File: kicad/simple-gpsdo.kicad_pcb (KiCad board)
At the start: 2 copper layers, 119.5 x 74.5 mm, 93 parts, among them J2 PWR, J3 ISP, J4 GPS_NEO, J5 GPS_IN, J6 10MHz_OUT, J7 NEO-6M, J8 10MHz_OUT, J9 USB_C_Receptacle_USB2.0, SW1 RST, U1 BD50FC0FP-E2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

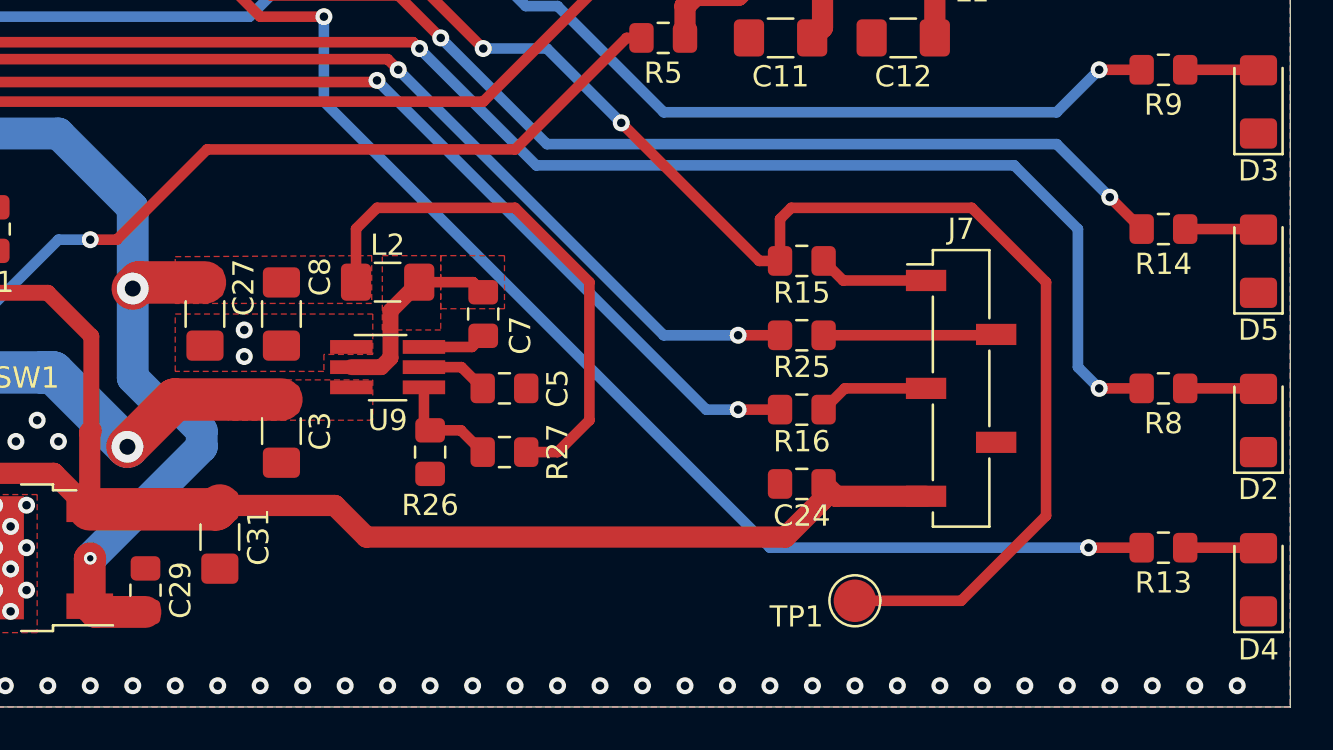
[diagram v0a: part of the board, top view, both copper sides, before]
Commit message: finalizing PCB, added 3D models
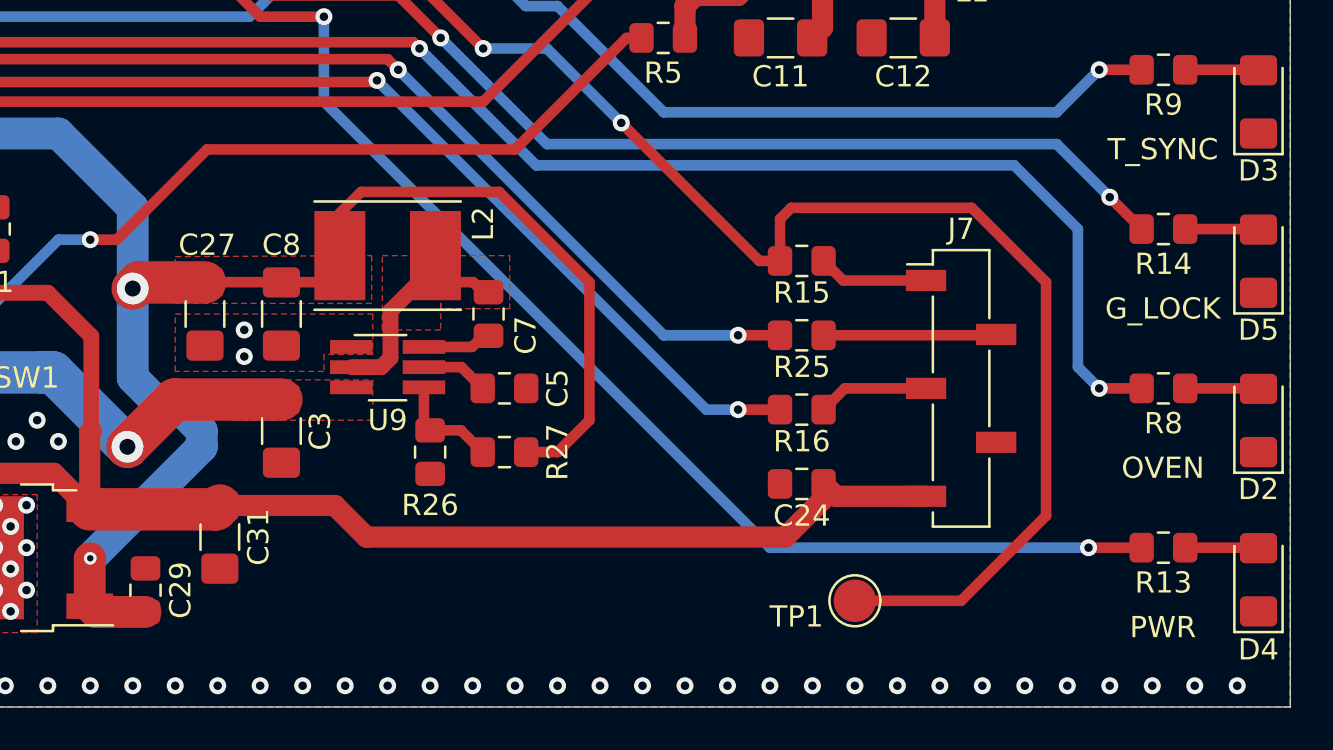
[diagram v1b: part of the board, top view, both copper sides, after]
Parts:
- L2: footprint Inductor_SMD:L_1206_3216Metric_Pad1.42x1.75mm_HandSolder -> Inductor_SMD:L_Taiyo-Yuden_NR-50xx_HandSoldering
- moved L2 1.25 mm to (152.0, 128.2)
- moved C7 0.25 mm to (156.8, 131.0)
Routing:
- net Net-(C27-Pad1): track 213.0 -> 224.2 mm
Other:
- board text added: "G_LOCK"
- board text added: "OVEN"
- board text added: "PWR"
- board text added: "T_SYNC"

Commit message: finalizing rev C PCB
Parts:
- moved J9 10.3 mm to (79.0, 122.8)
- moved R1 10.3 mm to (90.0, 121.2)
- moved R2 10.3 mm to (90.0, 124.2)
- moved J2 7.00 mm to (85.2, 130.5)
- moved F1 6.75 mm to (89.2, 130.3)
- moved FB1 6.75 mm to (93.2, 130.3)
- moved J6 2.25 mm to (91.5, 109.2)
- moved J8 2.25 mm to (91.5, 89.8)
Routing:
- net Net-(C3-Pad1): track 66.3 -> 59.9 mm
- net Net-(J9-PadA4): track 67.2 -> 61.1 mm
- net Net-(R2-Pad2): track 28.3 -> 22.6 mm
- net Net-(C27-Pad1): track 224.2 -> 229.0 mm
- net Net-(R1-Pad1): track 25.4 -> 22.7 mm
- net Net-(J8-Pad2): track 7.01 -> 9.26 mm, vias 0 -> 1
- net Net-(J6-Pad2): track 7.28 -> 9.53 mm, vias 0 -> 1
- net Net-(J8-Pad1): track 4.77 -> 2.63 mm
- net Net-(J6-Pad1): track 4.78 -> 2.66 mm
- net GND: vias 671 -> 676

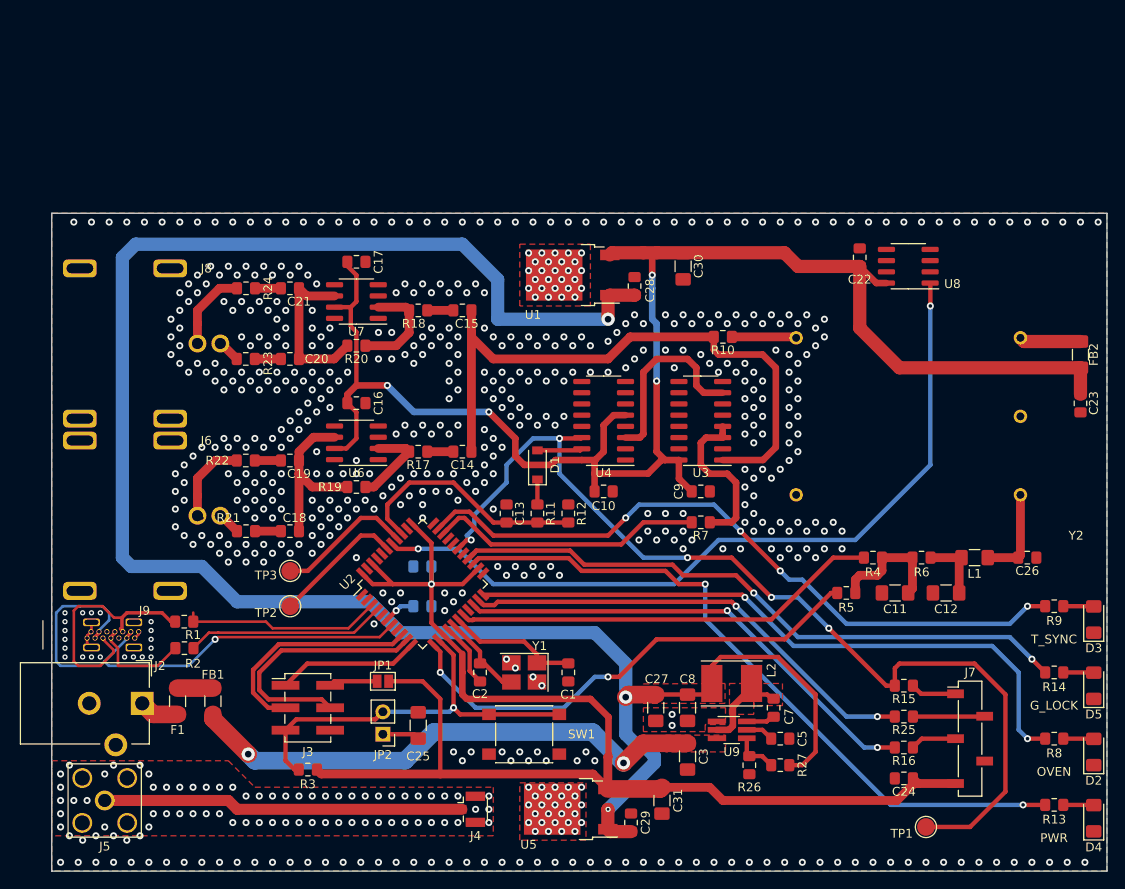
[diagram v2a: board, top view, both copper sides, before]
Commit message: added extra buck filtering
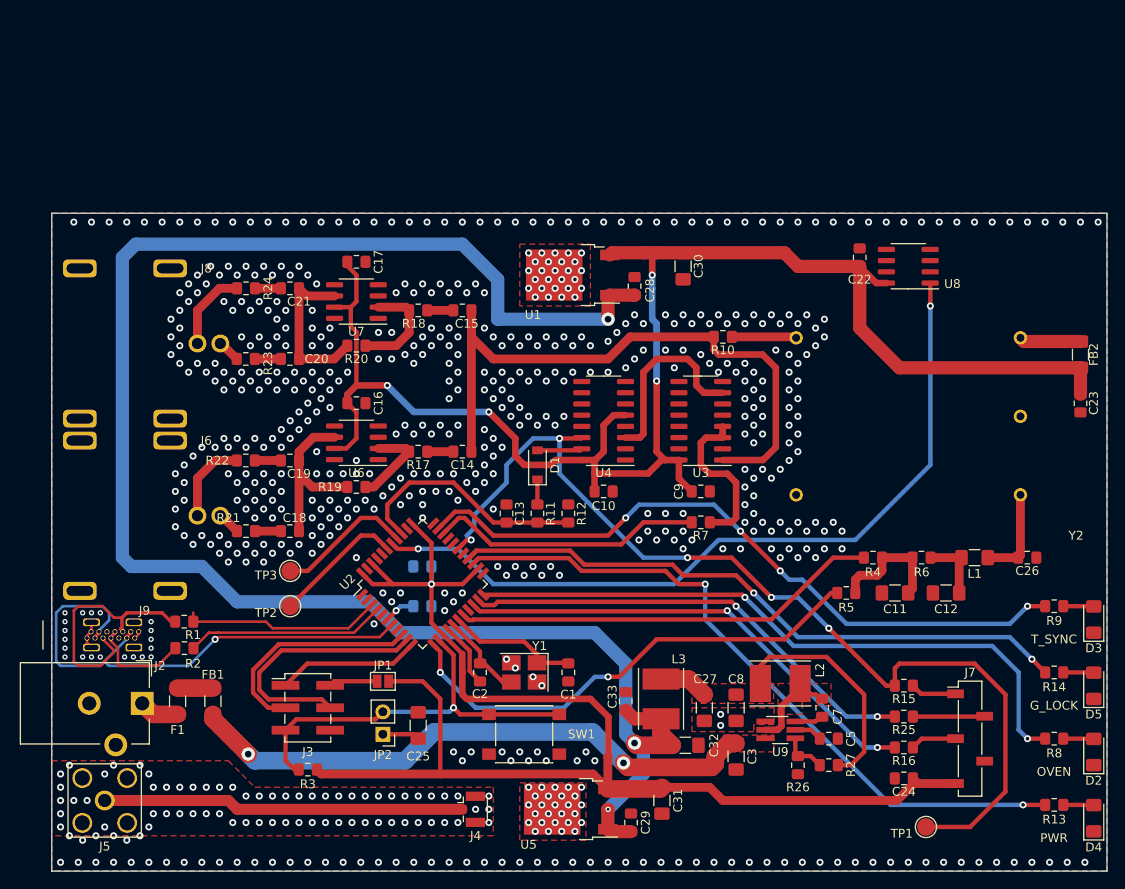
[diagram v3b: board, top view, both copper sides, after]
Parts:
- added C32: 10uF, Capacitor_SMD:C_1206_3216Metric_Pad1.42x1.75mm_HandSolder, F.Cu at (146.8, 135.2)
- added C33: 0.1uF, Capacitor_SMD:C_0805_2012Metric_Pad1.15x1.40mm_HandSolder, F.Cu at (140.0, 130.2)
- added L3: 3.3uH, Inductor_SMD:L_Taiyo-Yuden_NR-50xx_HandSoldering, F.Cu at (144.0, 130.0)
- J9: value USB_C_Receptacle_USB2.0 -> USB_C
- L1: value 33uH -> 3.3uH
- moved C27 5.50 mm to (148.9, 131.0)
- moved C3 5.50 mm to (152.5, 136.5)
- moved C5 5.50 mm to (163.0, 134.5)
- moved C7 5.50 mm to (162.2, 131.0)
- moved C8 5.50 mm to (152.5, 131.0)
- moved L2 5.50 mm to (157.5, 128.2)
- moved R26 5.50 mm to (159.5, 137.5)
- moved R27 5.50 mm to (163.0, 137.5)
- moved U9 5.50 mm to (157.5, 133.5)
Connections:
- C28 pad 2: Net-(C27-Pad1) -> +6V
- C29 pad 2: Net-(C27-Pad1) -> +6V
- U1 pad 1: Net-(C27-Pad1) -> +6V
- U5 pad 1: Net-(C27-Pad1) -> +6V
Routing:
- net +6V: track 0.00 -> 199.6 mm, vias 0 -> 3
- net Net-(C27-Pad1): track 229.0 -> 33.2 mm, vias 3 -> 0
- net Net-(C3-Pad1): track 59.9 -> 66.3 mm
- net Net-(J8-Pad2): vias 1 -> 0
- net Net-(J6-Pad2): vias 1 -> 0

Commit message: finalizing revC schematic and board
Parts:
- added J1: PPS_OUT, Connector_PinHeader_2.54mm:PinHeader_2x01_P2.54mm_Vertical, F.Cu at (95.8, 129.0)
- added Q1: DMP3099L, Package_TO_SOT_SMD:SOT-23_Handsoldering, F.Cu at (92.0, 136.5)
- moved FB1 1.00 mm to (92.2, 130.3)
- moved F1 0.25 mm to (89.0, 130.3)
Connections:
- FB1 pad 2: Net-(C3-Pad1) -> Net-(FB1-Pad2)
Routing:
- net GPS_PPS: track 112.0 -> 214.2 mm, vias 5 -> 6
- net Net-(FB1-Pad2): track 0.00 -> 5.47 mm
- net Net-(C3-Pad1): track 66.3 -> 64.2 mm
- net Net-(F1-Pad1): track 4.00 -> 3.25 mm
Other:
- board text added: "PPS"

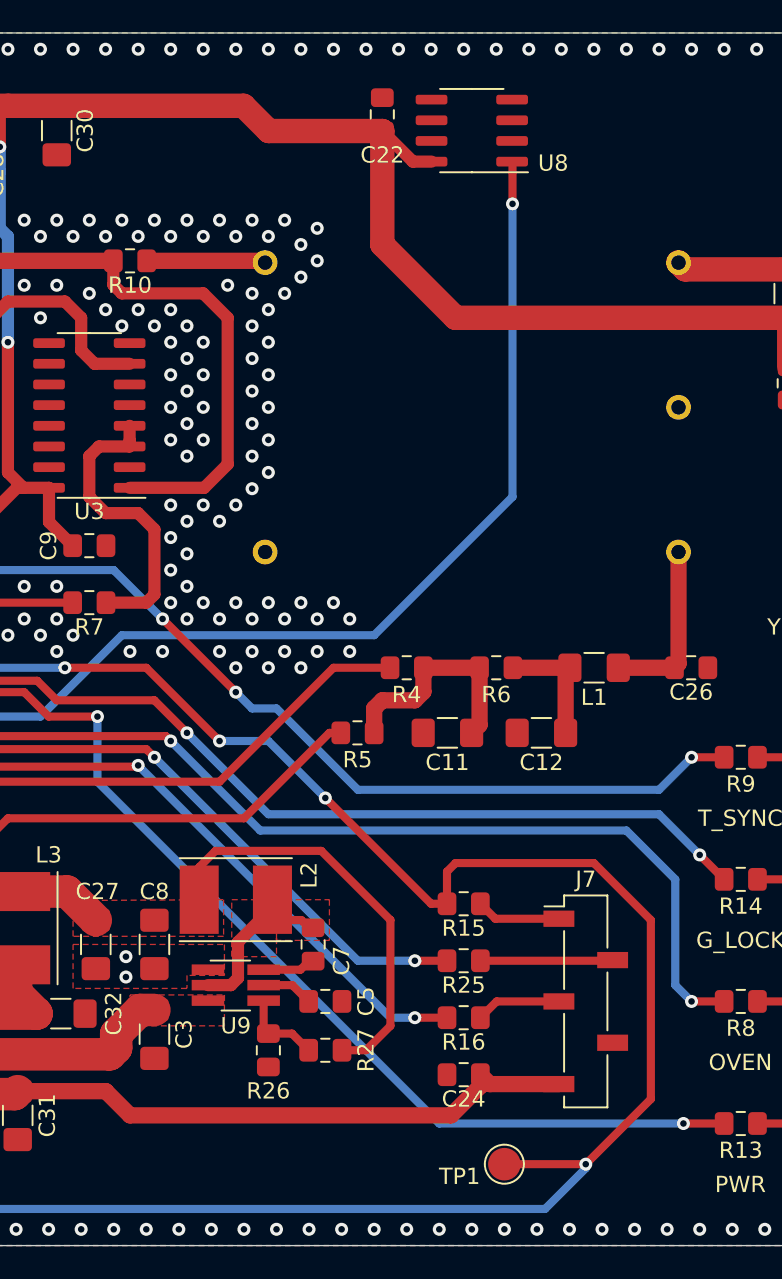
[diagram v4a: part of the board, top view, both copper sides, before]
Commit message: added filtering to LM35
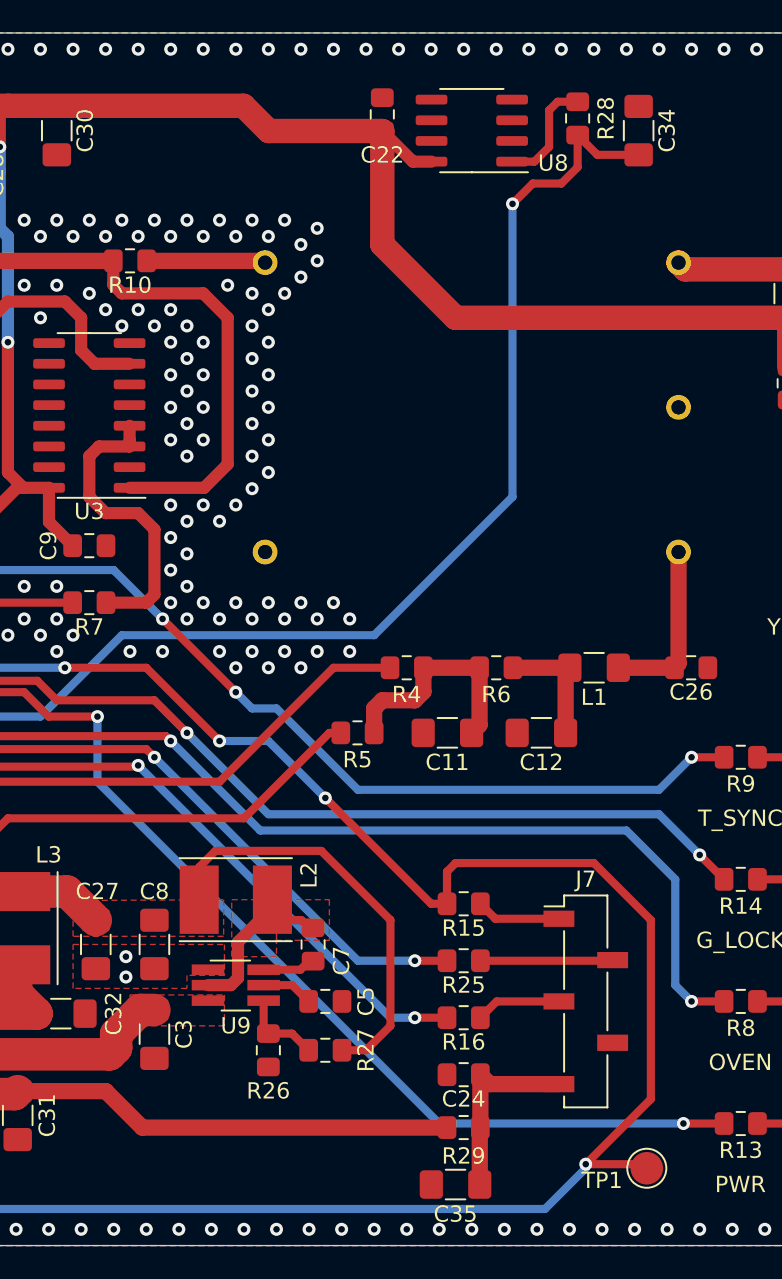
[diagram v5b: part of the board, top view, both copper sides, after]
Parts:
- added C34: 10uF, Capacitor_SMD:C_1206_3216Metric_Pad1.42x1.75mm_HandSolder, F.Cu at (182.2, 81.0)
- added C35: 10uF, Capacitor_SMD:C_1206_3216Metric_Pad1.42x1.75mm_HandSolder, F.Cu at (171.0, 145.8)
- added R28: 68R, Resistor_SMD:R_0805_2012Metric_Pad1.15x1.40mm_HandSolder, F.Cu at (178.5, 80.2)
- added R29: 2R, Resistor_SMD:R_0805_2012Metric_Pad1.15x1.40mm_HandSolder, F.Cu at (171.5, 142.2)
- moved TP1 8.75 mm to (182.8, 144.8)
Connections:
- C24 pad 2: +5VD -> Net-(C24-Pad2)
- J7 pad 5: +5VD -> Net-(C24-Pad2)
- U8 pad 1: /ADC2 -> Net-(R28-Pad2)
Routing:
- net Net-(C24-Pad2): track 0.00 -> 11.1 mm
- net /ADC2: track 89.1 -> 97.6 mm
- net +5VD: track 158.0 -> 149.7 mm
- net Net-(R28-Pad2): track 0.00 -> 6.90 mm
- net GPS_PPS: track 214.2 -> 213.0 mm

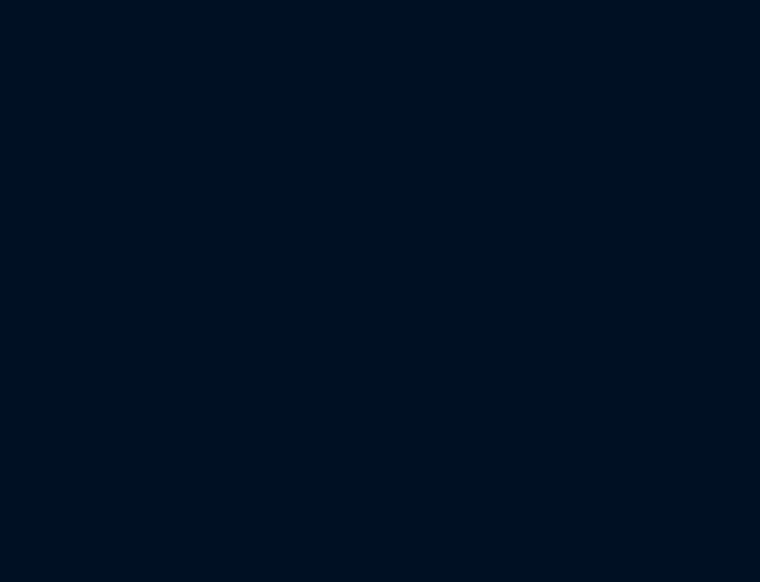
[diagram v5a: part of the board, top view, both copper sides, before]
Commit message: added fan control to schematic, board work still needed
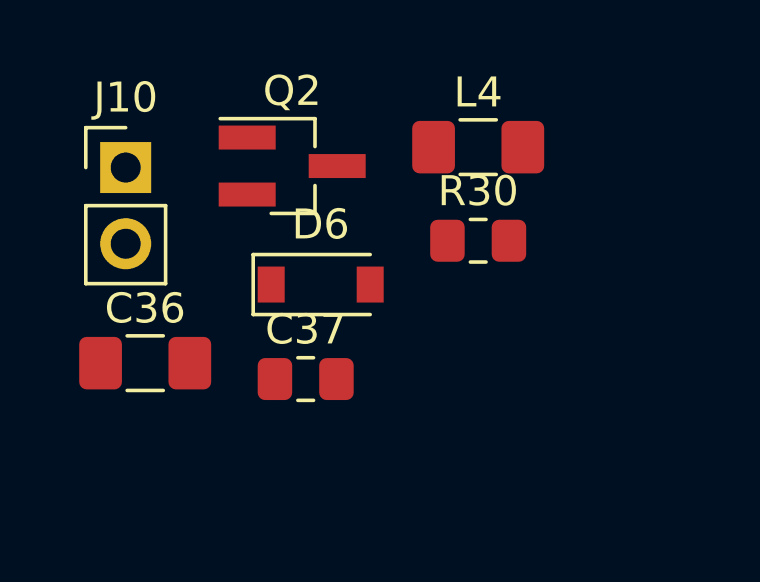
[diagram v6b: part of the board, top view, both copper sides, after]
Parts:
- added C36: 22uF, Capacitor_SMD:C_1206_3216Metric_Pad1.42x1.75mm_HandSolder, F.Cu at (74.2, 63.0)
- added C37: 0.1uF, Capacitor_SMD:C_0805_2012Metric_Pad1.15x1.40mm_HandSolder, F.Cu at (79.6, 63.5)
- added D6: 1N4148, Diode_SMD:D_SOD-123, F.Cu at (80.1, 60.3)
- added J10: FAN, Connector_PinHeader_2.54mm:PinHeader_1x02_P2.54mm_Vertical, F.Cu at (73.6, 56.4)
- added L4: 3.3uH, Inductor_SMD:L_1206_3216Metric_Pad1.42x1.75mm_HandSolder, F.Cu at (85.3, 55.8)
- added Q2: PMBT2222, Package_TO_SOT_SMD:SOT-23_Handsoldering, F.Cu at (79.1, 56.4)
- added R30: 1k, Resistor_SMD:R_0805_2012Metric_Pad1.15x1.40mm_HandSolder, F.Cu at (85.3, 58.9)
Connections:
- U2 pad 27: Net-(U2-Pad27) -> FAN_PWM

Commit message: finalizing revC updates
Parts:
- removed C36: 22uF, Capacitor_SMD:C_1206_3216Metric_Pad1.42x1.75mm_HandSolder
- removed C37: 0.1uF, Capacitor_SMD:C_0805_2012Metric_Pad1.15x1.40mm_HandSolder
- removed D6: 1N4148, Diode_SMD:D_SOD-123
- removed J10: FAN, Connector_PinHeader_2.54mm:PinHeader_1x02_P2.54mm_Vertical
- removed L4: 3.3uH, Inductor_SMD:L_1206_3216Metric_Pad1.42x1.75mm_HandSolder
- removed Q2: PMBT2222, Package_TO_SOT_SMD:SOT-23_Handsoldering
- removed R30: 1k, Resistor_SMD:R_0805_2012Metric_Pad1.15x1.40mm_HandSolder
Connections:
- U2 pad 27: FAN_PWM -> Net-(U2-Pad27)
